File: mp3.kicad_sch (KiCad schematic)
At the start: 38 parts, among them J1 AudioJack4_Ground, J2 AudioJack4_Ground, J3 Conn_01x08, J4 Micro_SD_Card_Det1, SW2 SW_Nidec_CAS-120A1, U1 XTAD5142IRGER, U2 MCP6002-xSN, U4 TP4056-42-ESOP8

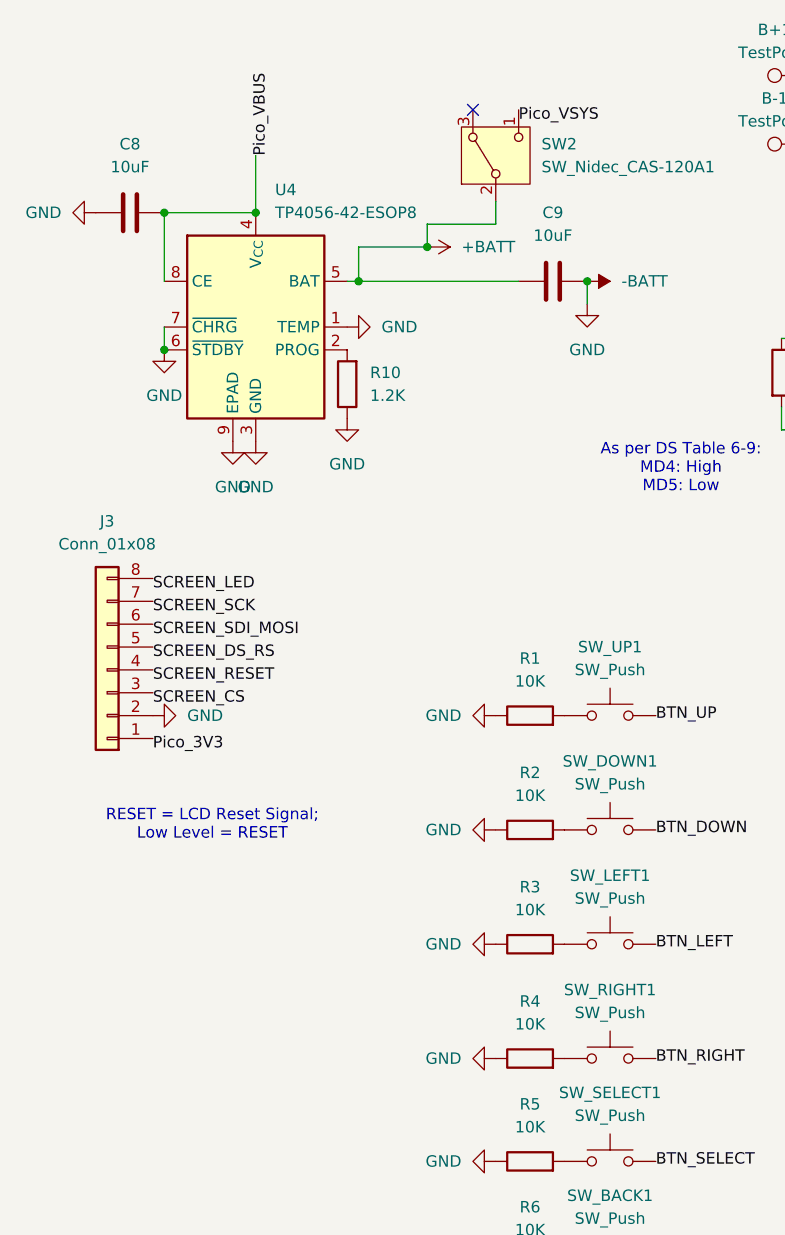
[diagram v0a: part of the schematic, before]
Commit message: Add voltage booster, optimizations
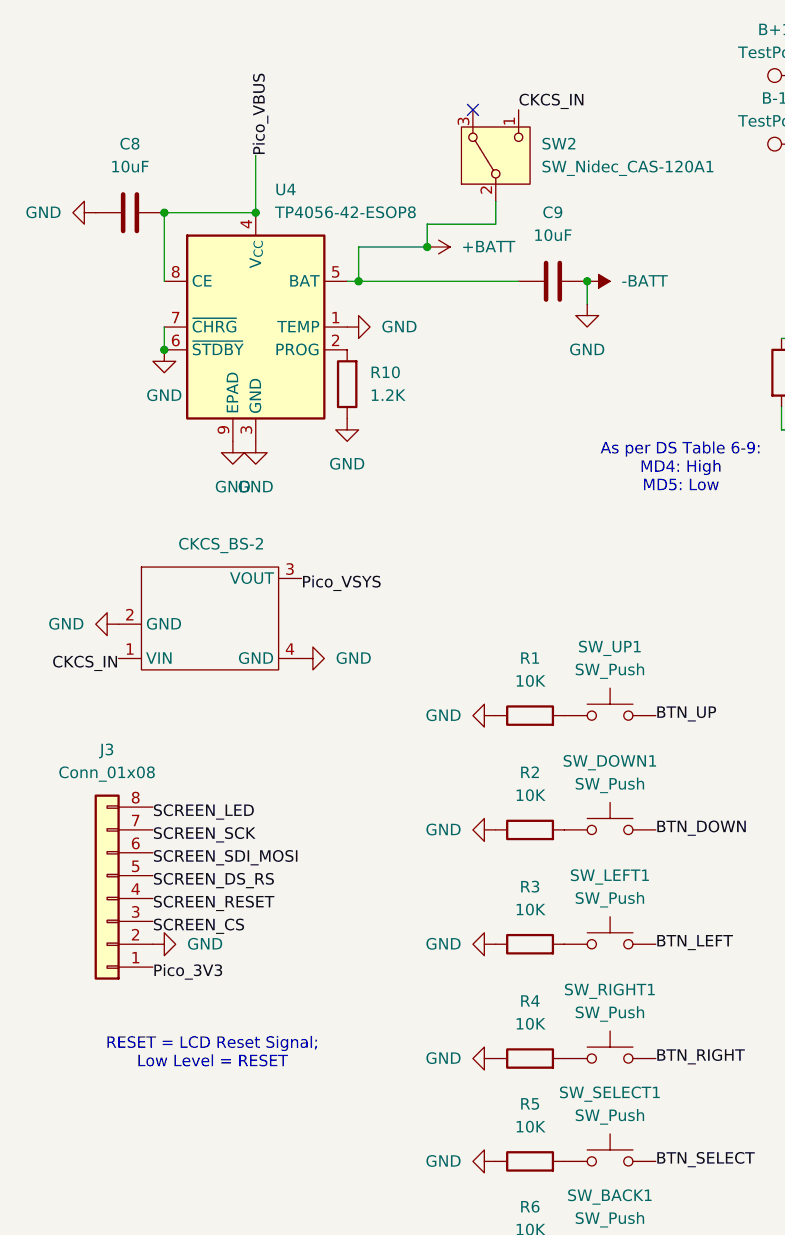
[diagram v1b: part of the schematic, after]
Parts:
- added CKCS_BS-2: (no value), CKCS_BS-01:CKCS_BS-01, symbol CKCS_BS-01:CKCS_BS-01_BOOSTER
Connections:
- net -BATT: now also CKCS_BS-2.2 (GND), CKCS_BS-2.4 (GND)
- net Pico_VSYS: now also CKCS_BS-2.3 (VOUT); no longer SW2.1 (C)
- new net CKCS_IN: CKCS_BS-2.1 (VIN), SW2.1 (C)
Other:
- moved on the sheet: J3

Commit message: Full re-routing
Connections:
- net at J2.4, U2.1, U2.2 (-): now also J1.4; no longer J1.3
- net at J2.3, U2.6 (-), U2.7: now also J1.3; no longer J1.4

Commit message: Fix diode direction
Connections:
- net Pico_VSYS: now also D1.1 (K); no longer D1.2 (A)
- net at A1.39 (VSYS): now also D1.2 (A); no longer D1.1 (K)
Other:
- moved on the sheet: D1
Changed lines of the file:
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@@
 	(symbol
 		(lib_id "Diode:1N5817")
-		(at 134.62 83.82 180)
+		(at 134.62 83.82 0)
 		(unit 1)
 		(body_style 1)
@@
 		(fields_autoplaced yes)
 		(property "Reference" "D1"
-			(at 134.9375 77.47 0)
+			(at 134.3025 77.47 0)
 			(show_name no)
 			(do_not_autoplace no)
@@
 		)
 		(property "Value" "1N5817"
-			(at 134.9375 80.01 0)
+			(at 134.3025 80.01 0)
 			(show_name no)
 			(do_not_autoplace no)
@@
 		)
 		(property "Footprint" "Diode_THT:D_DO-41_SOD81_P10.16mm_Horizontal"
-			(at 134.62 79.375 0)
+			(at 134.62 88.265 0)
 			(hide yes)
 			(show_name no)

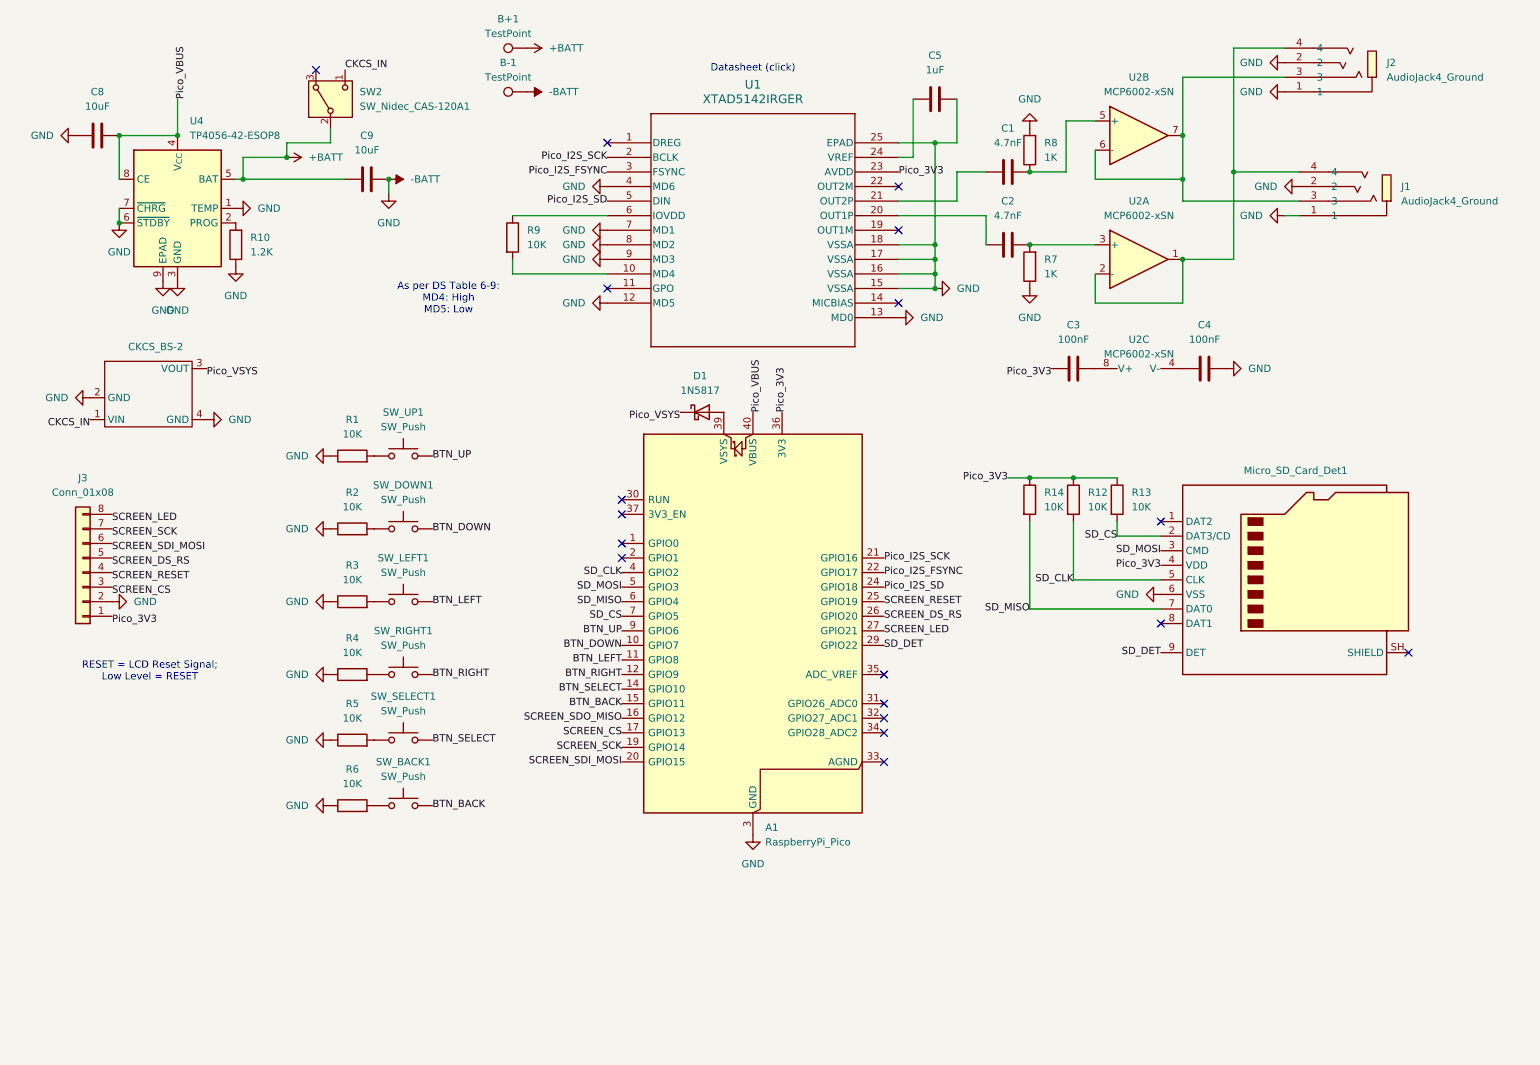
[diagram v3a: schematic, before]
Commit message: Add new battery management system
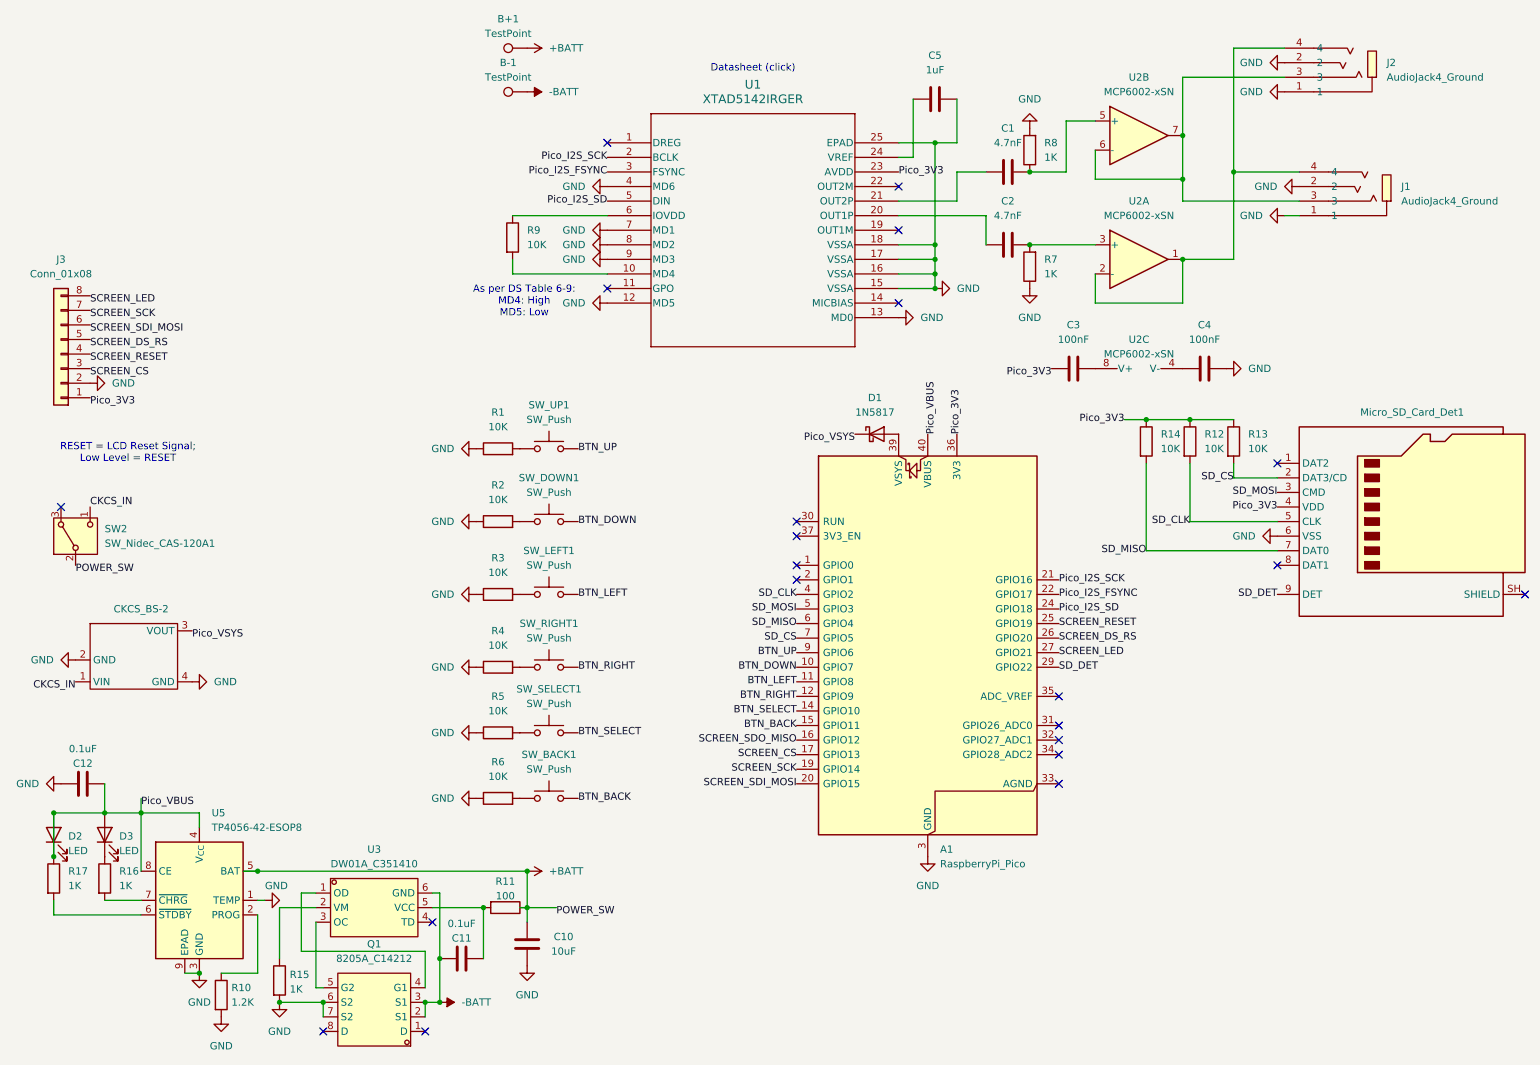
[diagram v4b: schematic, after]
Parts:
- removed C8, C9: 10uF, Capacitor_SMD:C_0402_1005Metric_Pad0.74x0.62mm_HandSolder, symbol Device:C
- removed U4: TP4056-42-ESOP8, Package_SO:SOIC-8-1EP_3.9x4.9mm_P1.27mm_EP2.41x3.3mm_ThermalVias, symbol Battery_Management:TP4056-42-ESOP8
- added C10: 10uF, Capacitor_SMD:C_0402_1005Metric_Pad0.74x0.62mm_HandSolder, symbol Device:C
- added C11, C12: 0.1uF, Capacitor_SMD:C_0402_1005Metric_Pad0.74x0.62mm_HandSolder, symbol Device:C
- added D2, D3: LED, symbol Device:LED
- added Q1: 8205A_C14212, JLCPCB_Misc:TSSOP-8_L4.4-W3.0-P0.65-LS6.4-BL-2, symbol JLCPCB_Misc:8205A_C14212
- added R11: 100, symbol Device:R
- added R15, R16, R17: 1K, symbol Device:R
- added U3: DW01A_C351410, JLCPCB_Power_Management_ICs:SOT-23-6_L2.9-W1.6-P0.95-LS2.8-BL, symbol JLCPCB_Power_Management_ICs:DW01A_C351410
- added U5: TP4056-42-ESOP8, Package_SO:SOIC-8-1EP_3.9x4.9mm_P1.27mm_EP2.41x3.3mm_ThermalVias, symbol Battery_Management:TP4056-42-ESOP8
- R10: footprint Resistor_SMD:R_0402_1005Metric -> (none)
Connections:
- net +BATT: now also C10.1, R11.1, U5.5 (BAT)
- net -BATT: now also C11.1, Q1.2 (S1), Q1.3 (S1), U3.6 (GND); no longer A1.13 (GND), A1.18 (GND), A1.23 (GND), A1.28 (GND), A1.3 (GND), A1.38 (GND), A1.8 (GND), C4.2, C5.1, CKCS_BS-2.2 (GND), CKCS_BS-2.4 (GND), J1.1, J1.2, J2.1, J2.2, J3.2 (Pin_2), J4.6 (VSS), R1.1, R10.1, R2.1, R3.1, R4.1, R5.1, R6.1, R7.1, R8.2, U1.12 (MD5), U1.13 (MD0), U1.15 (VSSA), U1.16 (VSSA), U1.17 (VSSA), U1.18 (VSSA), U1.25 (EPAD), U1.4 (MD6), U1.7 (MD1), U1.8 (MD2), U1.9 (MD3)
- net Pico_VBUS: now also C12.2, D2.1 (K), D2.2 (A), D3.2 (A), R17.1, U5.4 (V_{CC}), U5.8 (CE)
- net GND: now reaches R10.2
- net GND: now also A1.13 (GND), A1.18 (GND), A1.23 (GND), A1.28 (GND), A1.3 (GND), A1.38 (GND), A1.8 (GND), C4.2, C5.1, CKCS_BS-2.2 (GND), CKCS_BS-2.4 (GND), J1.1, J1.2, J2.1, J2.2, J3.2 (Pin_2), J4.6 (VSS), R1.1, R2.1, R3.1, R4.1, R5.1, R6.1, R7.1, R8.2, U1.12 (MD5), U1.13 (MD0), U1.15 (VSSA), U1.16 (VSSA), U1.17 (VSSA), U1.18 (VSSA), U1.25 (EPAD), U1.4 (MD6), U1.7 (MD1), U1.8 (MD2), U1.9 (MD3), C10.2, C12.1, Q1.6 (S2), Q1.7 (S2), R15.2, U5.1 (TEMP), U5.3 (GND), U5.9 (EPAD)
- new net: C11.2, R11.2, U3.5 (VCC)
- new net: Q1.4 (G1), U3.1 (OD)
- new net: Q1.5 (G2), U3.3 (OC)
- new net: R15.1, U3.2 (VM)
- new net: D3.1 (K), R16.1
- new net: R17.2, U5.6 (~{STDBY})
- new net: R10.1, U5.2 (PROG)
- new net: R16.2, U5.7 (~{CHRG})
- no-connect marks 18 -> 21
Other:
- moved on the sheet: A1, CKCS_BS-2, D1, J3, R1, R12, R13, R14, R2, R3, R4, R5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
